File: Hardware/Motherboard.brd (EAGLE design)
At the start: 124.5 x 73.7 mm, 78 parts, among them J1 MICROMOD-2222-C, J10 MICRO-SD-PUSH-PUSH-EXT-PIN, J2 Vertical Qwiic Connector, J4 QWIIC_RIGHT_ANGLE, J5 CORTEX_JTAG_DEBUG_MINIMUM_PTH, J6 MICROMOD_CARRIER, J7 MICROMOD_CARRIER, U2 MCP73831, U5 AP7361C-33

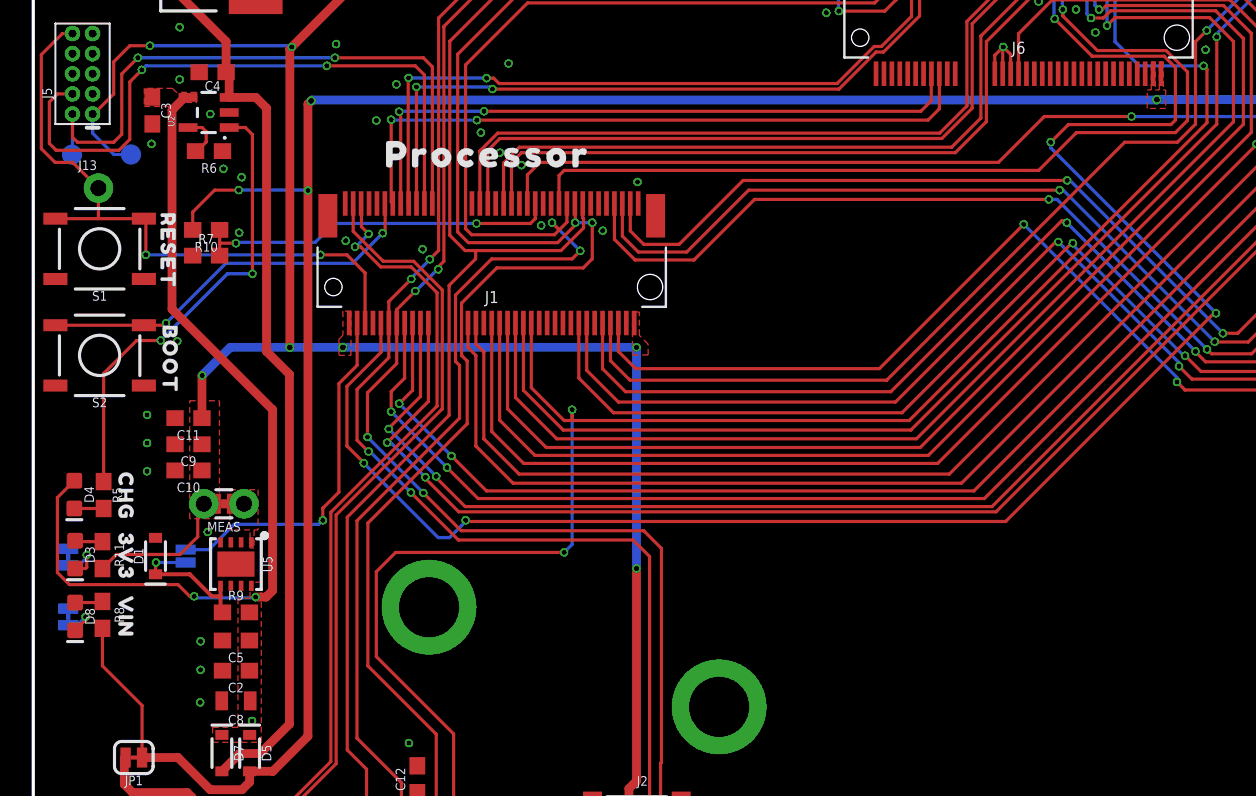
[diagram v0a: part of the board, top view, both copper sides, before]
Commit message: Adds second standoff for qwiic boards, attaches VIN net to processor connector
Deletes second page in schematic
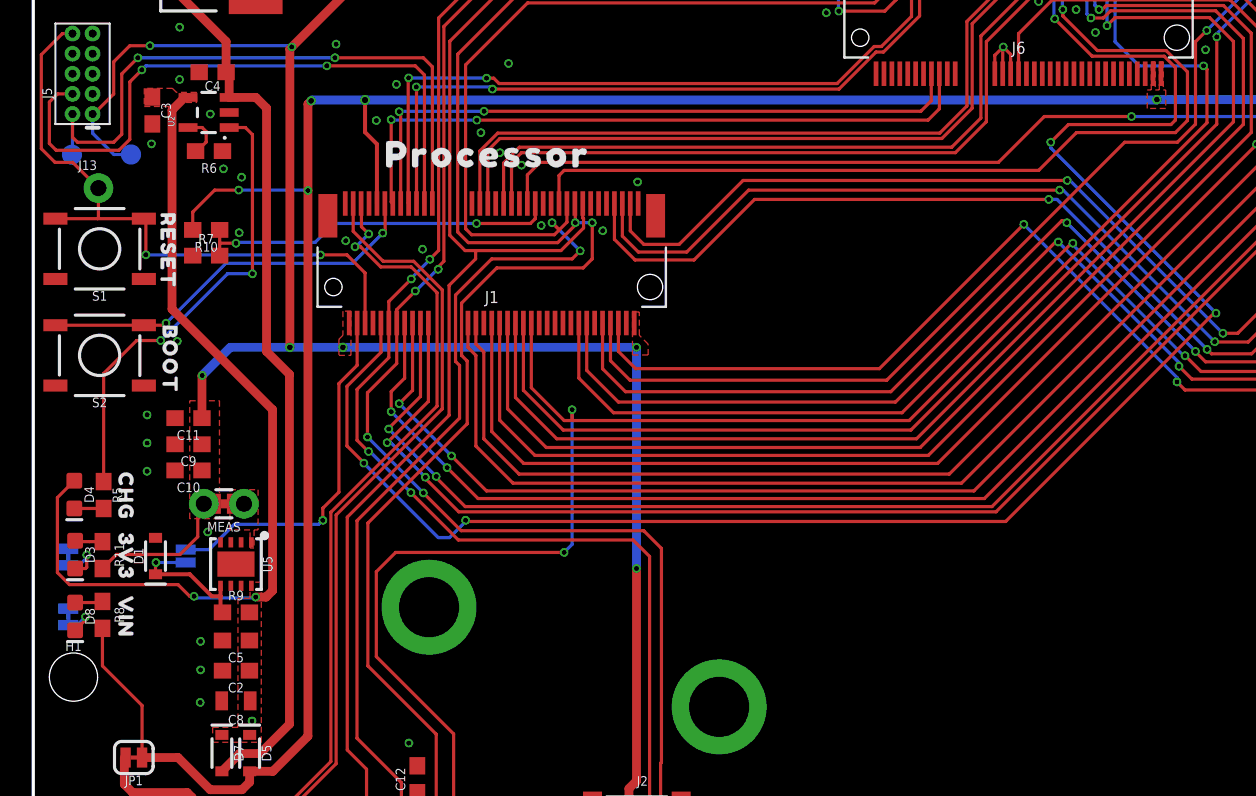
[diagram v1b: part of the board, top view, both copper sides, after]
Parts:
- added H1: STAND-OFFTIGHT, SparkFun-Hardware:STAND-OFF-TIGHT
- moved U$2 5.30 mm to (5.84, 30.5), turned to 0 degrees
- moved U$3 5.03 mm to (5.71, 26.7), turned to 0 degrees
- moved U$1 4.76 mm to (13.0, 30.5), turned to 0 degrees
- moved U$7 3.32 mm to (11.2, 13.0), turned to 0 degrees
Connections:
- removed net USB_VIN: J1.9
- net VIN: now also J1.9
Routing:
- net VIN: track 163.4 -> 170.2 mm, vias 7 -> 8
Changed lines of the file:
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@@
 <attribute name="VALUE" x="6.35" y="18.923" size="0.6096" layer="27" font="vector" ratio="20" rot="R180" align="top-center"/>
 </element>
-<element name="U$1" library="top" package="#3V3_EN#18" value="" x="9.652" y="33.909" smashed="yes" rot="MR270"/>
-<element name="U$2" library="top" package="#3V3_LED#17" value="" x="2.159" y="34.29" smashed="yes" rot="MR270"/>
-<element name="U$3" library="top" package="#VIN_LED#16" value="" x="2.286" y="22.987" smashed="yes" rot="MR90"/>
+<element name="U$1" library="top" package="#3V3_EN#18" value="" x="12.954" y="30.48" smashed="yes" rot="MR0"/>
+<element name="U$2" library="top" package="#3V3_LED#17" value="" x="5.842" y="30.48" smashed="yes" rot="MR0"/>
+<element name="U$3" library="top" package="#VIN_LED#16" value="" x="5.715" y="26.67" smashed="yes" rot="MR0"/>
 <element name="U$4" library="top" package="3V332533" value="" x="5.842" y="30.48" smashed="yes" rot="R270"/>
 <element name="U$5" library="top" package="VIN32532" value="" x="5.842" y="26.67" smashed="yes" rot="R270"/>
 <element name="U$6" library="top" package="CHG32531" value="" x="5.842" y="34.29" smashed="yes" rot="R270"/>
-<element name="U$7" library="top" package="#PTC#18" value="" x="8.89" y="15.367" smashed="yes" rot="MR270"/>
+<element name="U$7" library="top" package="#PTC#18" value="" x="11.176" y="12.954" smashed="yes" rot="MR0"/>
 <element name="U$8" library="top" package="BOOT32541" value="" x="8.636" y="42.926" smashed="yes" rot="R270"/>
 <element name="U$9" library="top" package="RESET32540" value="" x="8.509" y="49.784" smashed="yes" rot="R270"/>
@@
 <element name="LOGO2" library="SparkFun-Aesthetics" package="SFE_LOGO_NAME_FLAME_.3" value="SFE_LOGO_NAME_FLAME.3_INCH" x="62.23" y="33.02" smashed="yes" rot="MR0"/>
 <element name="LOGO3" library="SparkFun-Aesthetics" package="OSHW-LOGO-S" value="OSHW-LOGOS" x="120.65" y="7.62" smashed="yes" rot="MR0"/>
+<element name="H1" library="SparkFun-Hardware" package="STAND-OFF-TIGHT" value="STAND-OFFTIGHT" x="2.54" y="22.86" smashed="yes">
+<attribute name="NAME" x="2.54" y="24.511" size="0.6096" layer="25" font="vector" ratio="20" align="bottom-center"/>
+<attribute name="VALUE" x="2.54" y="21.209" size="0.6096" layer="27" font="vector" ratio="20" align="top-center"/>
+</element>
 </elements>
 <signals>
@@
 <wire x1="20.1676" y1="48.9966" x2="12.1666" y2="48.9966" width="0.2032" layer="16"/>
 </signal>
-<signal name="USB_VIN">
-<contactref element="J1" pad="9"/>
-</signal>
 <signal name="PROCESSOR_CAN-TX">
 <contactref element="J1" pad="43"/>
@@
 <vertex x="70.612" y="59.944"/>
 </polygon>
-<wire x1="17.6022" y1="59.309" x2="70.9422" y2="59.309" width="0.5588" layer="16"/>
+<wire x1="17.6022" y1="59.309" x2="20.955" y2="59.309" width="0.5588" layer="16"/>
+<wire x1="20.955" y1="59.309" x2="70.9422" y2="59.309" width="0.5588" layer="16"/>
 <wire x1="70.9422" y1="59.309" x2="70.9676" y2="59.3344" width="0.5588" layer="16"/>
 <via x="70.9676" y="59.3344" extent="1-16" drill="0.35"/>
@@
 <wire x1="11.176" y1="15.748" x2="9.144" y2="17.78" width="0.5588" layer="1"/>
 <wire x1="9.144" y1="17.78" x2="6.8707" y2="17.78" width="0.5588" layer="1"/>
+<contactref element="J1" pad="9"/>
+<wire x1="20.955" y1="57.277" x2="20.955" y2="59.309" width="0.254" layer="1"/>
+<via x="20.955" y="59.309" extent="1-16" drill="0.381"/>
+<wire x1="21.706" y1="52.773" x2="21.706" y2="56.526" width="0.254" layer="1"/>
+<wire x1="21.706" y1="56.526" x2="20.955" y2="57.277" width="0.254" layer="1"/>
 </signal>
 <signal name="SHLD">

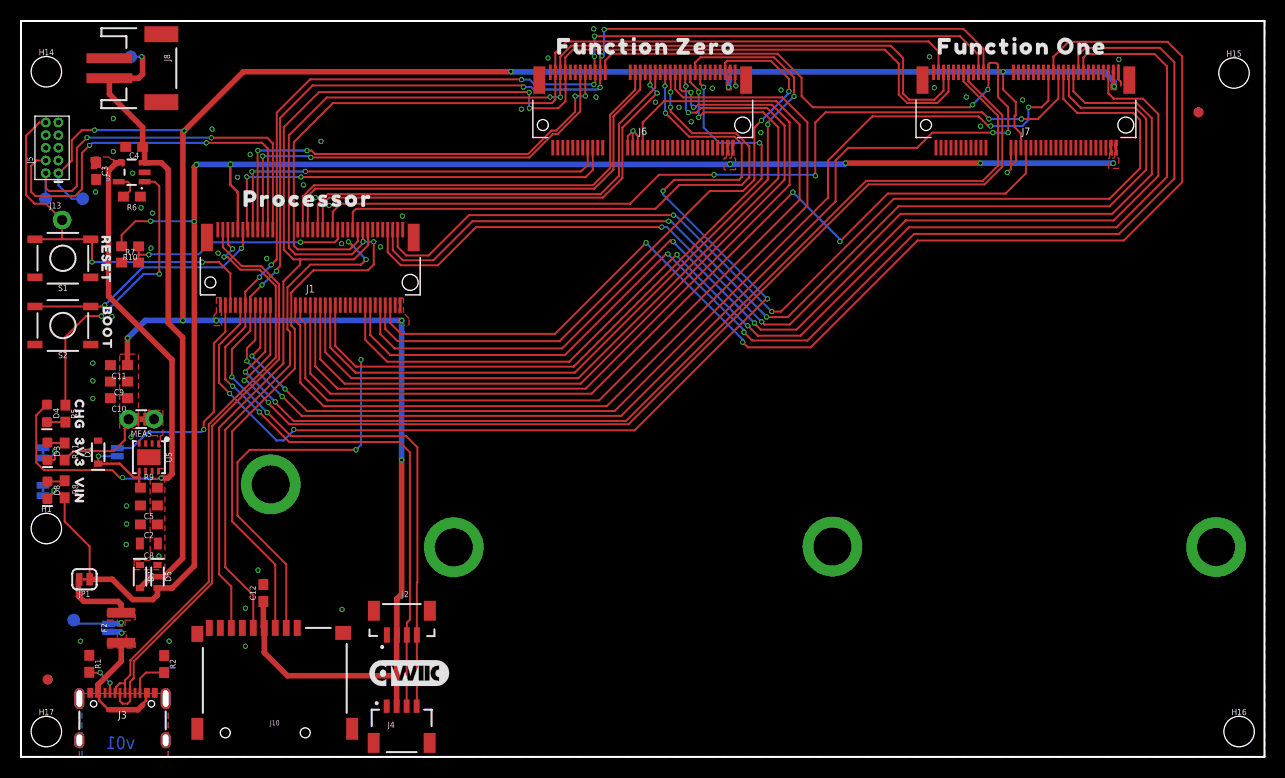
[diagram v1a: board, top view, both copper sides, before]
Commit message: Fixes trace routing
* Removes
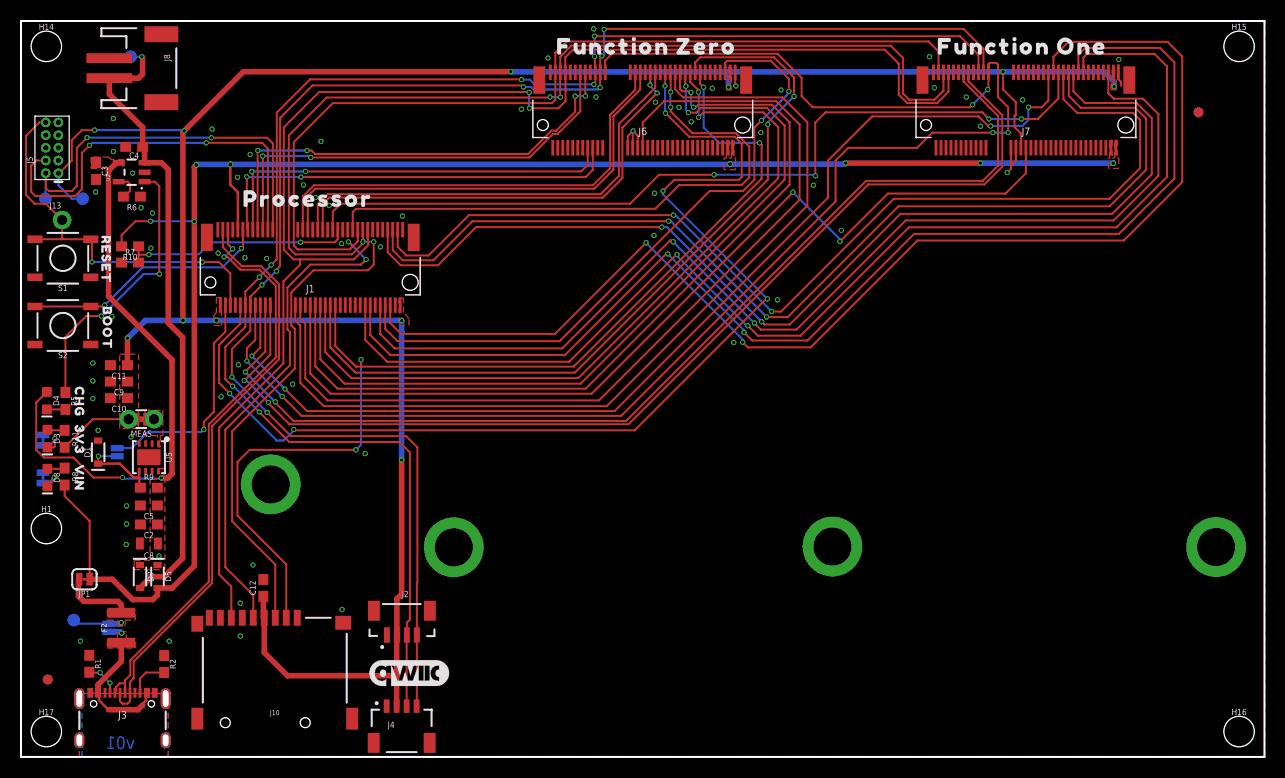
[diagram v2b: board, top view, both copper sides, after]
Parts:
- moved H15 2.71 mm to (121.9, 71.1)
- moved H14 2.54 mm to (2.54, 71.1)
- moved R5 1.27 mm to (4.45, 35.6)
- moved U$6 1.27 mm to (5.84, 35.6)
- moved 3V3_LED 1.27 mm to (2.21, 31.7)
- moved 5V_LED 1.27 mm to (2.21, 27.9)
- moved D3 1.27 mm to (2.64, 31.9)
- moved D8 1.27 mm to (2.64, 28.0)
- moved R11 1.27 mm to (4.37, 31.8)
- moved R8 1.27 mm to (4.37, 28.1)
- moved U$2 1.27 mm to (5.84, 31.8)
- moved U$3 1.27 mm to (5.71, 27.9)
- moved U$4 1.27 mm to (5.84, 31.8)
- moved U$5 1.27 mm to (5.84, 27.9)
- moved D4 1.27 mm to (2.59, 35.7)
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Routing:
- net VIN: track 170.2 -> 171.5 mm
- net N$15: track 29.3 -> 28.0 mm
- net SPI_PROCESSOR_SDO: track 149.8 -> 148.8 mm
- net SPI_PROCESSOR_SDI: track 145.1 -> 144.0 mm
- net SPI_PROCESSOR_SCK: track 142.6 -> 141.6 mm
- net G4-PROCESSOR/SD_CARD_!CS!: track 111.9 -> 110.9 mm
- net 3.3V: track 243.4 -> 242.4 mm
- net VCC: track 55.0 -> 55.5 mm
- net GND: vias 52 -> 64

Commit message: Adds silk, removes "VIN/VUSB" jumper
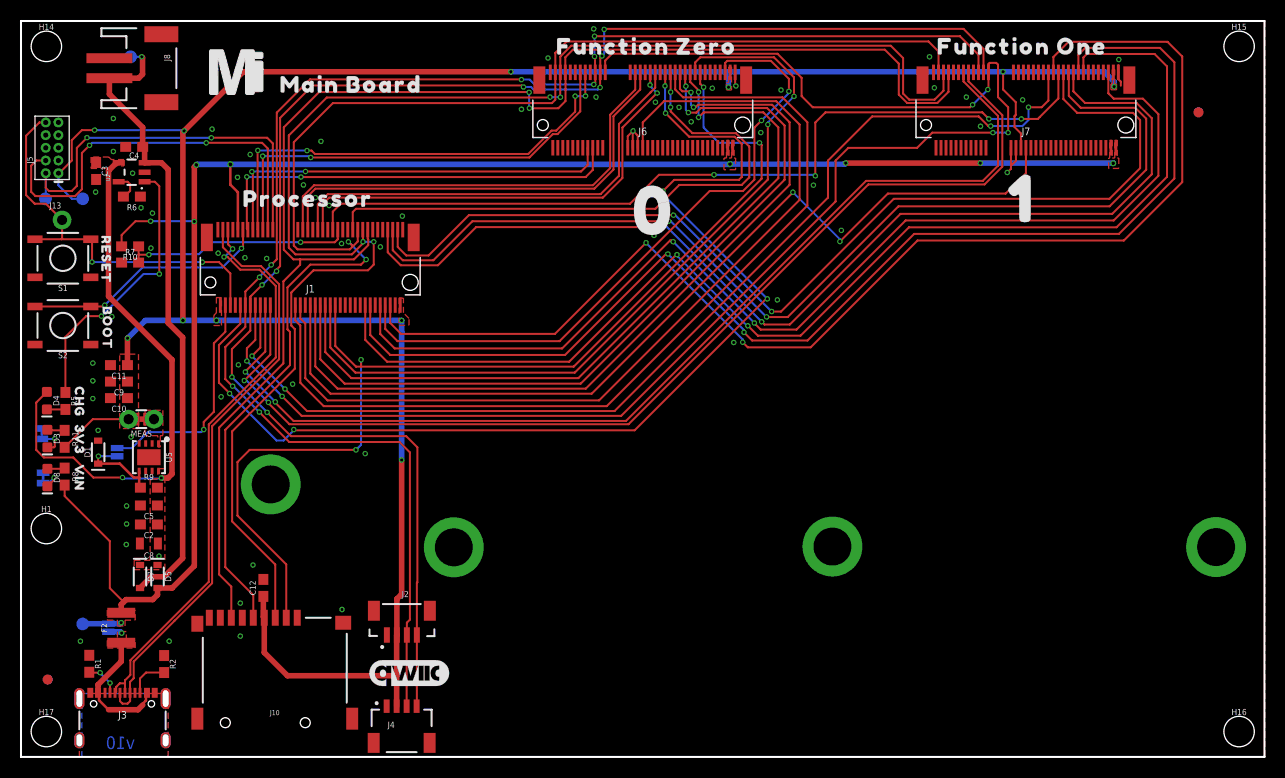
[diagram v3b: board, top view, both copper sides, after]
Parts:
- removed JP1: JUMPER-SMT_2_NC_TRACE_SILK, SparkFun-Jumpers:SMT-JUMPER_2_NC_TRACE_SILK
- added U$13: (no value), top:MAIN523
- added U$14: (no value), SparkFun-MicroMod:MICROMOD_MI_LOGO_1
- added U$15: (no value), top:0523
- added U$16: (no value), top:1524
- added U$17: (no value), top:MAIN_BOARD522
- added U$18: (no value), top:BOARD524
- moved TP4 0.97 mm to (6.17, 13.3)
- moved 3V3_LED 0.65 mm to (2.08, 32.3)
- moved U$2 0.65 mm to (5.71, 32.4)
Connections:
- removed net V_USB: BYP.2, F2.2, JP1.2, TP4.1
- net VIN: now also BYP.2, F2.2, TP4.1; no longer JP1.1
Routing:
- net V_USB: track 12.2 -> 0.00 mm, vias 1 -> 0
- net VIN: track 171.5 -> 176.1 mm, vias 8 -> 9
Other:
- board text added: "v10"
- board text removed: "v01"

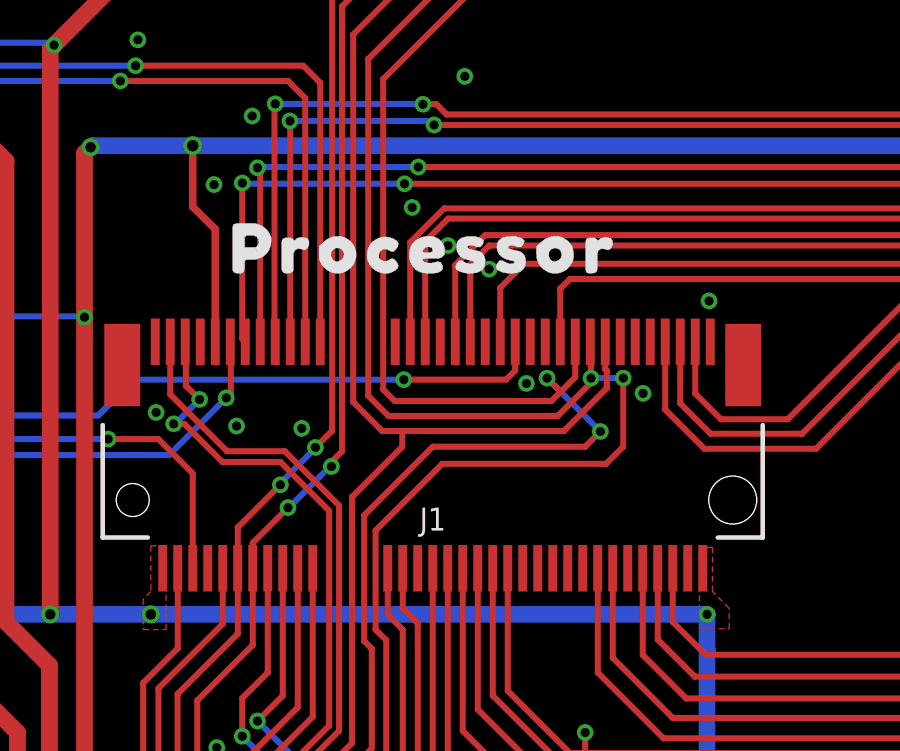
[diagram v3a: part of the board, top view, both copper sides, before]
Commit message: Double routes power enable for ESP32 processor boards
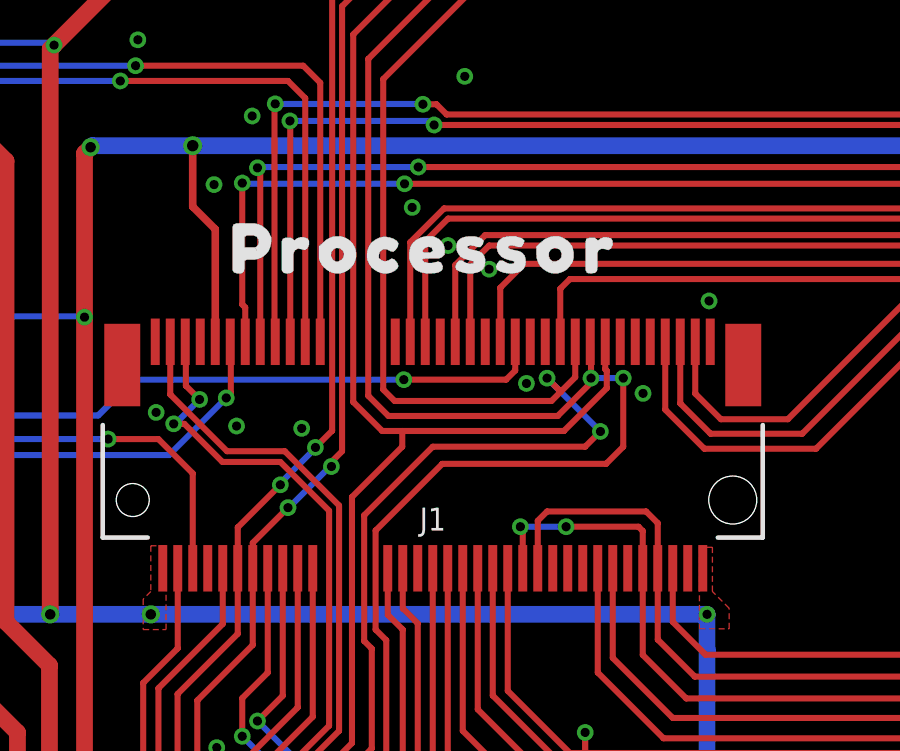
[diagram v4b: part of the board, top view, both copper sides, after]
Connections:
- net PWR_EN0: now also J1.52
- net PWR_EN1: now also J1.50
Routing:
- net PWR_EN0: track 66.2 -> 73.6 mm
- net PWR_EN1: track 110.1 -> 116.9 mm, vias 2 -> 4
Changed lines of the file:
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@@
 <wire x1="68.9315125" y1="56.642" x2="72.263" y2="56.642" width="0.2032" layer="1"/>
 <wire x1="53.9027125" y1="41.6132" x2="68.9315125" y2="56.642" width="0.2032" layer="1"/>
+<contactref element="J1" pad="52"/>
+<wire x1="36.456" y1="45.223" x2="36.456" y2="46.729" width="0.2032" layer="1"/>
+<wire x1="36.068" y1="47.117" x2="32.766" y2="47.117" width="0.2032" layer="1"/>
+<wire x1="32.766" y1="47.117" x2="32.456" y2="46.807" width="0.2032" layer="1"/>
+<wire x1="32.456" y1="46.807" x2="32.456" y2="45.223" width="0.2032" layer="1"/>
+<wire x1="36.456" y1="46.729" x2="36.068" y2="47.117" width="0.2032" layer="1"/>
 </signal>
 <signal name="PWR_EN1">
@@
 <wire x1="109.3724" y1="65.8876" x2="108.834" y2="66.426" width="0.2032" layer="1"/>
 <wire x1="108.834" y1="66.426" x2="108.834" y2="68.521" width="0.2032" layer="1"/>
+<contactref element="J1" pad="50"/>
+<wire x1="35.956" y1="45.223" x2="35.956" y2="46.467" width="0.2032" layer="1"/>
+<wire x1="35.956" y1="46.467" x2="35.814" y2="46.609" width="0.2032" layer="1"/>
+<wire x1="35.814" y1="46.609" x2="33.401" y2="46.609" width="0.2032" layer="1"/>
+<via x="33.401" y="46.609" extent="1-16" drill="0.3048"/>
+<wire x1="33.401" y1="46.609" x2="31.877" y2="46.609" width="0.2032" layer="16"/>
+<via x="31.877" y="46.609" extent="1-16" drill="0.3048"/>
+<wire x1="31.877" y1="46.609" x2="31.956" y2="46.53" width="0.2032" layer="1"/>
+<wire x1="31.956" y1="46.53" x2="31.956" y2="45.223" width="0.2032" layer="1"/>
 </signal>
 <signal name="I2C_SCL">
@@
 <contactref element="J1" pad="13"/>
 <contactref element="J6" pad="18"/>
-<wire x1="22.706" y1="52.773" x2="22.606" y2="52.873" width="0.2032" layer="1"/>
-<wire x1="22.606" y1="52.873" x2="22.606" y2="58.0644" width="0.2032" layer="1"/>
+<wire x1="22.706" y1="52.773" x2="22.706" y2="53.916" width="0.2032" layer="1"/>
+<wire x1="22.706" y1="53.916" x2="22.606" y2="54.016" width="0.2032" layer="1"/>
+<wire x1="22.606" y1="54.016" x2="22.606" y2="58.0644" width="0.2032" layer="1"/>
 <via x="22.606" y="58.0644" extent="1-16" drill="0.3048"/>
 <wire x1="28.0162" y1="58.039" x2="22.6314" y2="58.039" width="0.2032" layer="16"/>

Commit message: Rename polygon to VIN to match the trace, approves some overlap errors
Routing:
- removed copper zone on layer 1, net V_USB
